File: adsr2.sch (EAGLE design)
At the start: 47 parts, among them IC1 LM324D, IC2 4066D, IC3 4555D, SW1 TL2285, SW2 TL2285, T1 BC847, T2 BC857

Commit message: Board added. Status LEDs removed (only GATE indicator left)
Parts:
- removed C10: 1u, rcl:C-EUC1206K
- removed LED1, LED2, LED3: (no value), led:LED3MM
- removed R6, R7, R8: 1k, rcl:R-EU_R0603
- removed SW1, SW2: TL2285, lb_devs:TL2285
- added GATE_THRU: WQP-PJ301M-12_JACK, thonkiconn:WQP-PJ301M-12_JACK
- added R15: 470, rcl:R-EU_R0603
- added R22, R23: 1k, rcl:R-EU_R0603
- added R24: 3k3, rcl:R-EU_R0603
- added SW1_TIME, SW2_TRIG: TL2285, lb_devs:TL2285
- C11, C12: value 10u -> 4u7
- C7: value 1u -> 470n
- R1: value 33 -> 470
- R17: value 100k -> 1k; device pot-alps:POT_USVERTICAL -> rcl:R-EU_R0603
- R18: value 3k9 -> 39k
- R19: device rcl:R-EU_R1206 -> rcl:R-EU_R0603
- R2: value 10k -> 100k
- R21: value 10k -> 4k7
- renumbered ATT_OUT to OUT1, OUT to OUT2
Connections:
- removed net N$21 (its old number): IC1C.-IN, IC1C.OUT, R16.2
- removed net N$4: LED3.A, R8.1
- removed net N$8: LED2.A, R7.1
- removed net N$9: LED1.A, R6.1
- new net N$13: IC1C.+IN, R21.2, R24.1
- new net N$14: GATE_THRU.2, R17.1
- new net N$15: R22.2, R4.S
- new net N$23: R23.2, R3.S
- new net N$28: R15.1, R5.S
- net ATTACK: now also SW2_TRIG.P3; no longer R7.2, SW2.P3
- net DEC_SUST: no longer R8.2
- net ENV_CAP: now also IC1B.+IN, SW1_TIME.P2; no longer C10.1, IC1D.+IN, SW1.P2
- net GND: now also GATE_THRU.1, R24.2; no longer C10.2, LED1.C, LED2.C, LED3.C, R17.A, R21.2
- net N$10: now also R15.2; no longer R5.S
- net N$12: now also IC1B.-IN, IC1B.OUT, R16.2; no longer IC1D.-IN, IC1D.OUT, R17.E
- net N$16: now also SW1_TIME.P3; no longer SW1.P3
- net N$18: now also SW1_TIME.P1; no longer SW1.P1
- net N$24: now also IC1C.-IN, IC1C.OUT, R17.2; no longer IC1C.+IN, R17.S
- net N$27: now also SW2_TRIG.P2; no longer SW2.P2
- net N$5: now also R23.1; no longer R3.S
- net N$6: now also R22.1; no longer R4.S
- net N$7: now also IC1D.-IN, IC1D.OUT; no longer IC1B.-IN, IC1B.OUT
- net RELEASE: no longer R6.2
- net SUST_LEVEL: now also IC1D.+IN; no longer IC1B.+IN
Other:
- note added: "Gated / Triggered Attack (press -> triggered, always completes attack phase even if gate goes low/off)"
- note added: "Note: Only one of C11/C12 need to be fitted. They are there to enable different form factor (0603 or 1206) caps on the PCB."
- note added: "R15, R22, R23: Current limiting resistors The CD4066 is limited to 10mA."
- note removed: "Gated / Triggered Attack (press -> triggered, always completes attack phase)"
- note removed: "Note: Only one of C7/C10 and C11/C12 need to be fitted. They are there to enable different form factor (0603 or 1206) caps on the PCB."
- moved on the sheet: C1, C11, C12, C7, D1, D3, D4, D5, IC1B, IC1C, IC1D, IC3A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

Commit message: Changed gate IO and outputs: Gate in, Gate thru, "Attack done" trigger out, Envelope CV Out. Removed gate thru mode selector switch. Added LED #2 for "attack done" trigger. Adjusted component labels on PCB. Added D2, prevents current leak back from diode logic surrounding IC3A to attack_done signal (affects gate output circuit if not there).
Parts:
- removed OUT1, OUT2: WQP-PJ301M-12_JACK, thonkiconn:WQP-PJ301M-12_JACK
- added AT_TRIG, CV_OUT: WQP-PJ301M-12_JACK, thonkiconn:WQP-PJ301M-12_JACK
- added D2: 1N4148, adafruit:DIODESOD-323F
- added LED1: AT_TRIG_LED, led:LED3MM
- added R25, R6, R7: 100k, rcl:R-EU_R0603
- added R26, R8: 4k7, rcl:R-EU_R0603
- added R27: 3k3, rcl:R-EU_R0603
- added SW_MANUAL: TL2285, lb_devs:TL2285
- added T3, T5: BC857, transistor:BC857A-PNP-SOT23-BEC
- added T4: BC847, transistor:BC847
- R16: value 1k -> 3k3
- R17: value 1k -> 100k
- R21: value 4k7 -> 10k
- R24: value 3k3 -> 10k
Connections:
- removed net N$14: GATE_THRU.2, R17.1
- new net N$29: D2.C, R14.1
- new net N$30: R24.2, R25.1, T4.C
- new net N$31: LED1.C, R24.1
- new net N$33: R25.2, T5.B
- new net N$34: R26.1, T5.C
- new net N$35: AT_TRIG.2, R26.2, R27.1
- new net N$4: R6.2, SW_MANUAL.P4
- new net N$8: R7.2, T3.B
- new net N$9: R8.1, T3.C
- net +12V: now also LED1.A, SW_MANUAL.P5, T3.E, T5.E
- net ATTACK_DONE: now also D2.A, R17.2; no longer R14.1
- net GATE_IN: now also R7.1
- net GND: now also AT_TRIG.1, CV_OUT.1, IC1C.+IN, R16.2, R21.2, R27.2, T4.E; no longer OUT1.1, OUT2.1, R24.2
- net N$11: now also CV_OUT.2; no longer OUT2.2
- net N$12: no longer R16.2
- net N$13: now also GATE_THRU.2, R16.1, R8.2; no longer IC1C.+IN, R21.2, R24.1
- net N$19: now also R17.1, T4.B; no longer OUT1.2, R16.1
- net N$21: now also R6.1
- net N$24: no longer R17.2
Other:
- note added: "TL2285 latching Gated / Triggered Attack (press -> triggered, always completes attack phase even if gate goes low/off)"
- note added: "TL2285 momentary Manual trigger button"
- note removed: "Gated / Triggered Attack (press -> triggered, always completes attack phase even if gate goes low/off)"
- moved on the sheet: C1, C11, C12, C13, C7, C8, C9, D1, D3, D4, D5, GATE_IN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

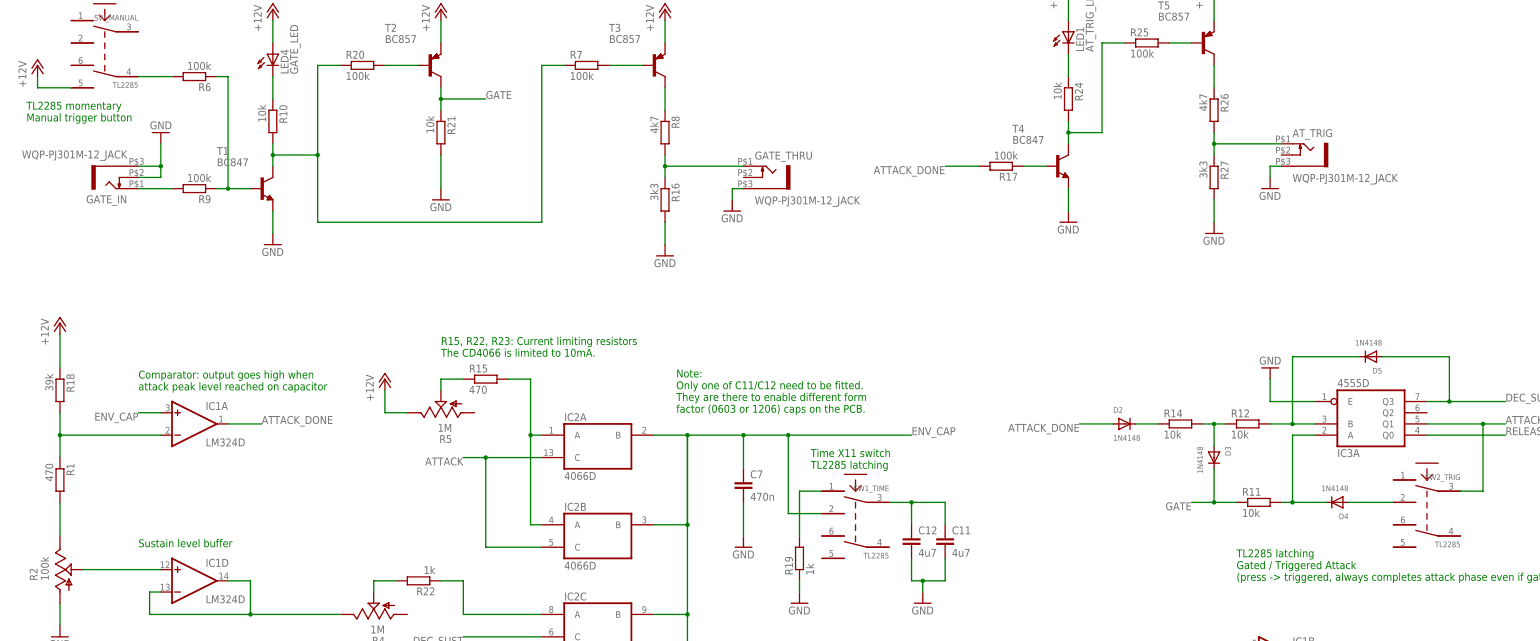
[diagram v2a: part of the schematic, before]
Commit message: Minor routing fixes & components moved.
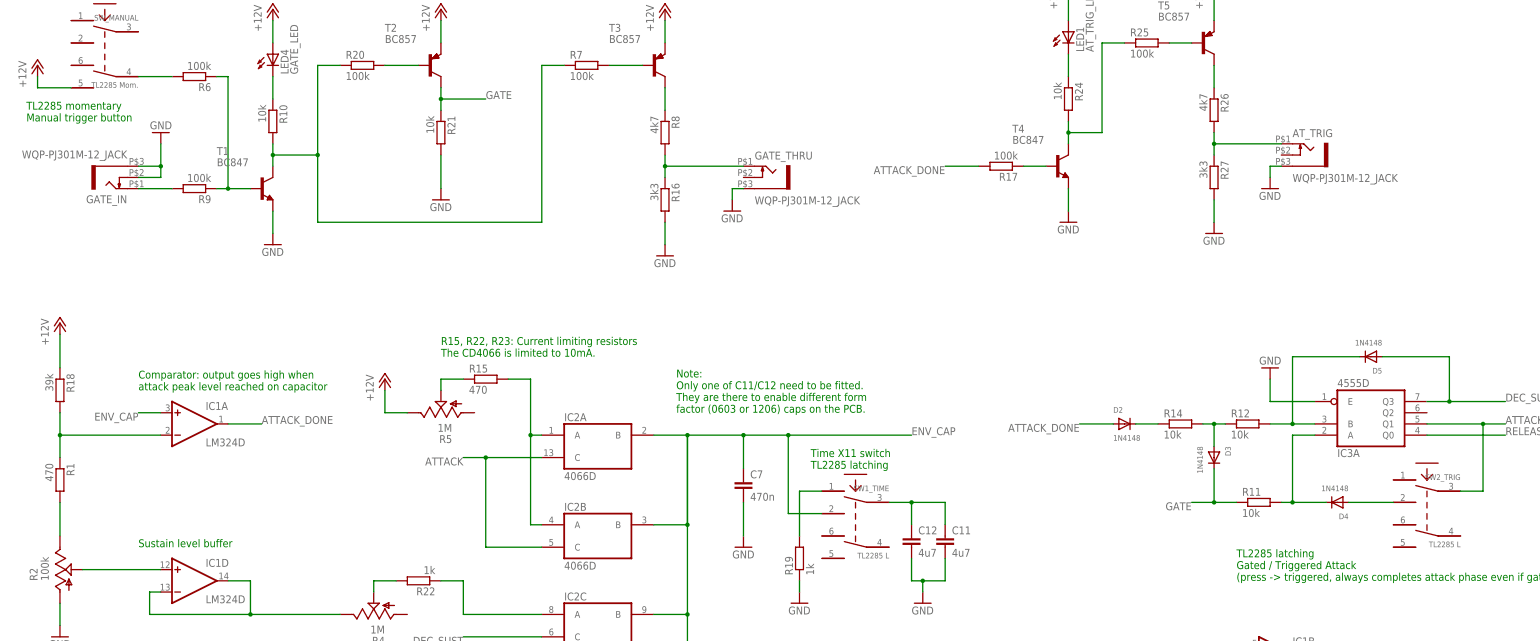
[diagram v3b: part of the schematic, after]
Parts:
- SW1_TIME, SW2_TRIG: value TL2285 -> TL2285 L
- SW_MANUAL: value TL2285 -> TL2285 Mom.
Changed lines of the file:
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@@
 <part name="CV_OUT" library="thonkiconn" deviceset="WQP-PJ301M-12_JACK" device=""/>
 <part name="GND16" library="supply1" deviceset="GND" device=""/>
-<part name="SW1_TIME" library="lb_devs" deviceset="TL2285" device=""/>
+<part name="SW1_TIME" library="lb_devs" deviceset="TL2285" device="" value="TL2285 L"/>
 <part name="C11" library="rcl" deviceset="C-EU" device="C1206K" value="4u7"/>
 <part name="C12" library="rcl" deviceset="C-EU" device="C0603K" value="4u7"/>
@@
 <part name="D4" library="adafruit" deviceset="DIODE" device="SOD-323F" value="1N4148"/>
 <part name="D5" library="adafruit" deviceset="DIODE" device="SOD-323F" value="1N4148"/>
-<part name="SW2_TRIG" library="lb_devs" deviceset="TL2285" device=""/>
+<part name="SW2_TRIG" library="lb_devs" deviceset="TL2285" device="" value="TL2285 L"/>
 <part name="P+7" library="supply1" deviceset="+12V" device=""/>
 <part name="R15" library="rcl" deviceset="R-EU_" device="R0603" value="470"/>
@@
 <part name="GATE_THRU" library="thonkiconn" deviceset="WQP-PJ301M-12_JACK" device=""/>
 <part name="GND8" library="supply1" deviceset="GND" device=""/>
-<part name="SW_MANUAL" library="lb_devs" deviceset="TL2285" device=""/>
+<part name="SW_MANUAL" library="lb_devs" deviceset="TL2285" device="" value="TL2285 Mom."/>
 <part name="R6" library="rcl" deviceset="R-EU_" device="R0603" value="100k"/>
 <part name="P+8" library="supply1" deviceset="+12V" device=""/>

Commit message: Changed some resistors from 100k to 10k; this works with the used BC847 transistors. (Breadboard prototype used BC547B)
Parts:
- R20, R25, R7, R9: value 100k -> 10k
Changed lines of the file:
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@@
 <grid distance="0.1" unitdist="inch" unit="inch" style="lines" multiple="1" display="no" altdistance="0.01" altunitdist="inch" altunit="inch"/>
 <layers>
-<layer number="1" name="Top" color="4" fill="1" visible="yes" active="no"/>
-<layer number="16" name="Bottom" color="1" fill="1" visible="yes" active="no"/>
-<layer number="17" name="Pads" color="2" fill="1" visible="yes" active="no"/>
-<layer number="18" name="Vias" color="2" fill="1" visible="yes" active="no"/>
-<layer number="19" name="Unrouted" color="14" fill="1" visible="yes" active="no"/>
-<layer number="20" name="Dimension" color="15" fill="1" visible="yes" active="no"/>
-<layer number="21" name="tPlace" color="7" fill="1" visible="yes" active="no"/>
-<layer number="22" name="bPlace" color="7" fill="1" visible="yes" active="no"/>
-<layer number="23" name="tOrigins" color="15" fill="1" visible="yes" active="no"/>
-<layer number="24" name="bOrigins" color="15" fill="1" visible="yes" active="no"/>
-<layer number="25" name="tNames" color="7" fill="1" visible="yes" active="no"/>
-<layer number="26" name="bNames" color="7" fill="1" visible="yes" active="no"/>
-<layer number="27" name="tValues" color="7" fill="1" visible="yes" active="no"/>
-<layer number="28" name="bValues" color="7" fill="1" visible="yes" active="no"/>
+<layer number="1" name="Top" color="4" fill="1" visible="no" active="no"/>
+<layer number="16" name="Bottom" color="1" fill="1" visible="no" active="no"/>
+<layer number="17" name="Pads" color="2" fill="1" visible="no" active="no"/>
+<layer number="18" name="Vias" color="2" fill="1" visible="no" active="no"/>
+<layer number="19" name="Unrouted" color="14" fill="1" visible="no" active="no"/>
+<layer number="20" name="Dimension" color="15" fill="1" visible="no" active="no"/>
+<layer number="21" name="tPlace" color="7" fill="1" visible="no" active="no"/>
+<layer number="22" name="bPlace" color="7" fill="1" visible="no" active="no"/>
+<layer number="23" name="tOrigins" color="15" fill="1" visible="no" active="no"/>
+<layer number="24" name="bOrigins" color="15" fill="1" visible="no" active="no"/>
+<layer number="25" name="tNames" color="7" fill="1" visible="no" active="no"/>
+<layer number="26" name="bNames" color="7" fill="1" visible="no" active="no"/>
+<layer number="27" name="tValues" color="7" fill="1" visible="no" active="no"/>
+<layer number="28" name="bValues" color="7" fill="1" visible="no" active="no"/>
 <layer number="29" name="tStop" color="7" fill="3" visible="no" active="no"/>
 <layer number="30" name="bStop" color="7" fill="6" visible="no" active="no"/>
@@
 <layer number="35" name="tGlue" color="7" fill="4" visible="no" active="no"/>
 <layer number="36" name="bGlue" color="7" fill="5" visible="no" active="no"/>
-<layer number="37" name="tTest" color="7" fill="1" visible="yes" active="no"/>
-<layer number="38" name="bTest" color="7" fill="1" visible="yes" active="no"/>
+<layer number="37" name="tTest" color="7" fill="1" visible="no" active="no"/>
+<layer number="38" name="bTest" color="7" fill="1" visible="no" active="no"/>
 <layer number="39" name="tKeepout" color="4" fill="11" visible="no" active="no"/>
 <layer number="40" name="bKeepout" color="1" fill="11" visible="no" active="no"/>
@@
 <layer number="44" name="Drills" color="7" fill="1" visible="no" active="no"/>
 <layer number="45" name="Holes" color="7" fill="1" visible="no" active="no"/>
-<layer number="46" name="Milling" color="3" fill="1" visible="yes" active="no"/>
-<layer number="47" name="Measures" color="7" fill="1" visible="yes" active="no"/>
-<layer number="48" name="Document" color="7" fill="1" visible="yes" active="no"/>
-<layer number="49" name="Reference" color="7" fill="1" visible="yes" active="no"/>
-<layer number="50" name="dxf" color="7" fill="1" visible="yes" active="no"/>
-<layer number="51" name="tDocu" color="7" fill="1" visible="yes" active="no"/>
-<layer number="52" name="bDocu" color="7" fill="1" visible="yes" active="no"/>
-<layer number="53" name="tGND_GNDA" color="7" fill="9" visible="yes" active="no"/>
-<layer number="54" name="bGND_GNDA" color="1" fill="9" visible="yes" active="no"/>
-<layer number="56" name="wert" color="7" fill="1" visible="yes" active="no"/>
-<layer number="57" name="tCAD" color="7" fill="1" visible="yes" active="no"/>
+<layer number="46" name="Milling" color="3" fill="1" visible="no" active="no"/>
+<layer number="47" name="Measures" color="7" fill="1" visible="no" active="no"/>
+<layer number="48" name="Document" color="7" fill="1" visible="no" active="no"/>
+<layer number="49" name="Reference" color="7" fill="1" visible="no" active="no"/>
+<layer number="50" name="dxf" color="7" fill="1" visible="no" active="no"/>
+<layer number="51" name="tDocu" color="7" fill="1" visible="no" active="no"/>
+<layer number="52" name="bDocu" color="7" fill="1" visible="no" active="no"/>
+<layer number="53" name="tGND_GNDA" color="7" fill="9" visible="no" active="no"/>
+<layer number="54" name="bGND_GNDA" color="1" fill="9" visible="no" active="no"/>
+<layer number="56" name="wert" color="7" fill="1" visible="no" active="no"/>
+<layer number="57" name="tCAD" color="7" fill="1" visible="no" active="no"/>
 <layer number="90" name="Modules" color="5" fill="1" visible="yes" active="yes"/>
 <layer number="91" name="Nets" color="2" fill="1" visible="yes" active="yes"/>
@@
 <part name="GND7" library="supply1" deviceset="GND" device=""/>
 <part name="GATE_IN" library="thonkiconn" deviceset="WQP-PJ301M-12_JACK" device=""/>
-<part name="R9" library="rcl" deviceset="R-EU_" device="R0603" value="100k"/>
+<part name="R9" library="rcl" deviceset="R-EU_" device="R0603" value="10k"/>
 <part name="T1" library="transistor" deviceset="BC847" device=""/>
 <part name="R10" library="rcl" deviceset="R-EU_" device="R0603" value="10k"/>
@@
 <part name="P+5" library="supply1" deviceset="+12V" device=""/>
 <part name="LED4" library="led" deviceset="LED" device="3MM" value="GATE_LED"/>
-<part name="R20" library="rcl" deviceset="R-EU_" device="R0603" value="100k"/>
+<part name="R20" library="rcl" deviceset="R-EU_" device="R0603" value="10k"/>
 <part name="T2" library="transistor" deviceset="*-PNP-" device="SOT23-BEC" technology="BC857A" value="BC857"/>
 <part name="P+6" library="supply1" deviceset="+12V" device=""/>
@@
 <part name="D2" library="adafruit" deviceset="DIODE" device="SOD-323F" value="1N4148"/>
 <part name="GND9" library="supply1" deviceset="GND" device=""/>
-<part name="R7" library="rcl" deviceset="R-EU_" device="R0603" value="100k"/>
+<part name="R7" library="rcl" deviceset="R-EU_" device="R0603" value="10k"/>
 <part name="T3" library="transistor" deviceset="*-PNP-" device="SOT23-BEC" technology="BC857A" value="BC857"/>
 <part name="P+9" library="supply1" deviceset="+12V" device=""/>
@@
 <part name="LED1" library="led" deviceset="LED" device="3MM" value="AT_TRIG_LED"/>
 <part name="P+10" library="supply1" deviceset="+12V" device=""/>
-<part name="R25" library="rcl" deviceset="R-EU_" device="R0603" value="100k"/>
+<part name="R25" library="rcl" deviceset="R-EU_" device="R0603" value="10k"/>
 <part name="T5" library="transistor" deviceset="*-PNP-" device="SOT23-BEC" technology="BC857A" value="BC857"/>
 <part name="R26" library="rcl" deviceset="R-EU_" device="R0603" value="4k7"/>
